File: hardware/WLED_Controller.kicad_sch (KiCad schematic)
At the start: 79 parts, among them J1 Conn_01x01_Male, J11 Conn_01x01_Male, J12 Conn_01x01_Male, J2 USB_B_Micro, J3 Conn_01x01_Male, J4 Conn_01x01_Male, J5 Conn_01x01_Male, Q1 S8050_SMD, Q2 S8050_SMD, Q3 2N7002, Q4 2N7002, SW1 SW_SPST, SW2 SW_SPST, U1 AMS1117-3.3, U2 AMS1117-3.3, U3 TP4056, U4 ESP-12F, U5 CP2102N-A01-GQFN28, U6 AP2007, U7 AP2007, U8 AP2007

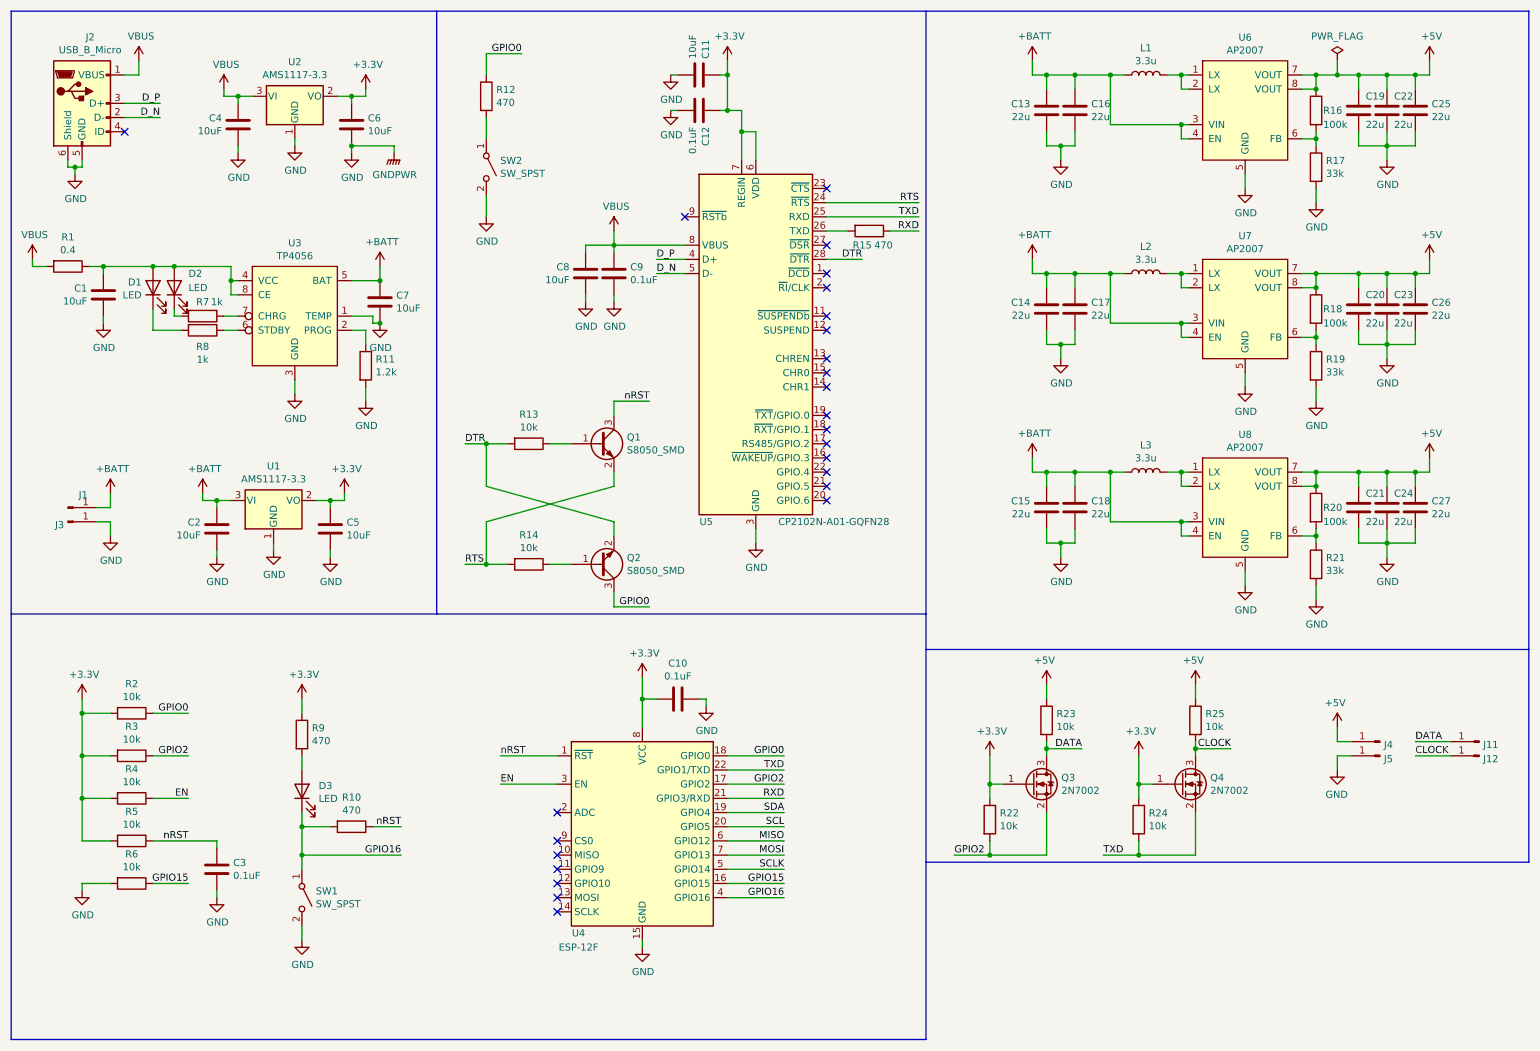
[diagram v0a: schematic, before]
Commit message: Updated to v2.0.0
Contains the PCB design and fabrication files for v2.0.0 of the WLED
controller.
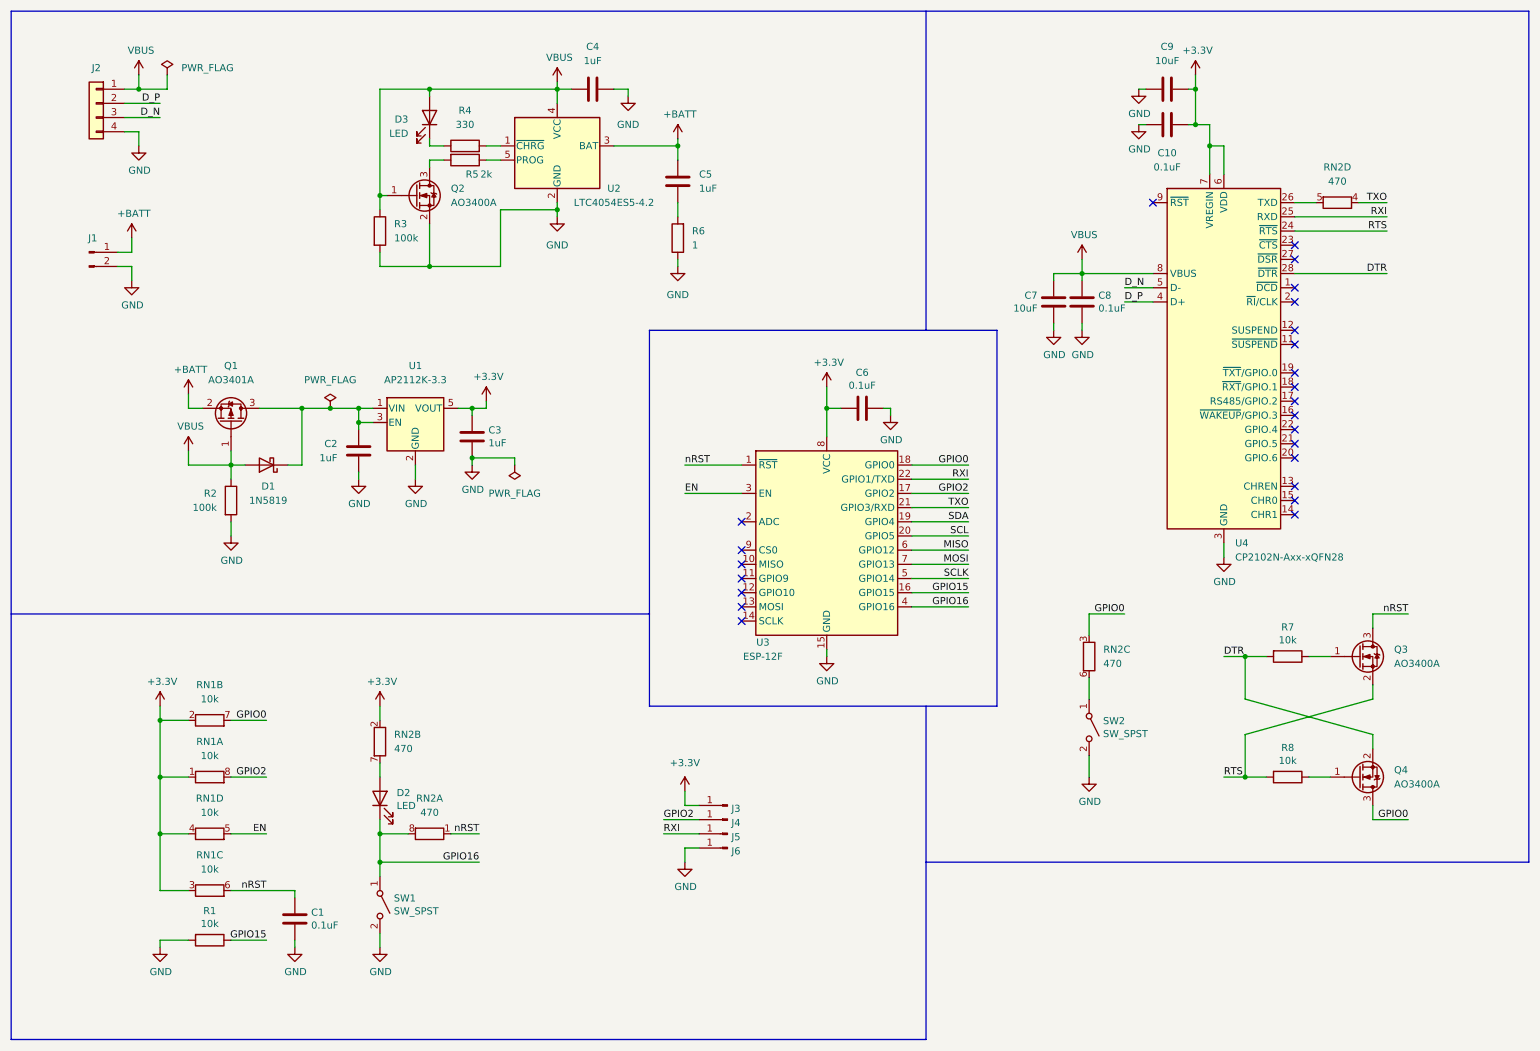
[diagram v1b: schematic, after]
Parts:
- removed C1, C11, C6: 10uF, Capacitor_SMD:C_0805_2012Metric, symbol Device:C
- removed C12: 0.1uF, Capacitor_SMD:C_0805_2012Metric, symbol Device:C
- removed C13, C14, C15, C16, C17, C18, C19, C20, C21, C22, C23, C24, C25, C26, C27: 22u, Capacitor_SMD:C_0805_2012Metric, symbol Device:C
- removed D1, D2: LED, LED_SMD:LED_0805_2012Metric, symbol Device:LED
- removed J1, J4, J5: Conn_01x01_Male, Connector_Wire:SolderWirePad_1x01_SMD_5x10mm, symbol Connector:Conn_01x01_Male
- removed J2: USB_B_Micro, Connector_USB:USB_Micro-B_Molex_47346-0001, symbol Connector:USB_B_Micro
- removed L1, L2, L3: 3.3u, Inductor_SMD:L_1206_3216Metric, symbol Device:L
- removed Q1, Q2: S8050_SMD, Package_TO_SOT_SMD:SOT-23, symbol New_Library:S8050_SMD
- removed Q3, Q4: 2N7002, Package_TO_SOT_SMD:SOT-23, symbol Transistor_FET:2N7002
- removed R1: 0.4, Resistor_SMD:R_1210_3225Metric, symbol Device:R
- removed R10, R12, R15, R9: 470, Resistor_SMD:R_0805_2012Metric, symbol Device:R
- removed R11: 1.2k, Resistor_SMD:R_0805_2012Metric, symbol Device:R
- removed R16, R18, R20: 100k, Resistor_SMD:R_0805_2012Metric, symbol Device:R
- removed R17, R19, R21: 33k, Resistor_SMD:R_0805_2012Metric, symbol Device:R
- removed R22, R23, R24, R25: 10k, Resistor_SMD:R_0805_2012Metric, symbol Device:R
- removed R7, R8: 1k, Resistor_SMD:R_0805_2012Metric, symbol Device:R
- removed U1, U2: AMS1117-3.3, Package_TO_SOT_SMD:SOT-223, symbol Regulator_Linear:AMS1117-3.3
- removed U3: TP4056, myfootprints:SOP-8-EP_3.9x4.9mm_P1.27mm, symbol New_Library:TP4056
- removed U5: CP2102N-A01-GQFN28, Package_DFN_QFN:QFN-28-1EP_5x5mm_P0.5mm_EP3.35x3.35mm, symbol Interface_USB:CP2102N-A01-GQFN28
- removed U6, U7, U8: AP2007, myfootprints:SOP-8-EP_3.9x4.9mm_P1.27mm, symbol New_Library:AP2007
- added C10: 0.1uF, Capacitor_SMD:C_0603_1608Metric, symbol Device:C
- added C3: 1uF, Capacitor_SMD:C_0603_1608Metric, symbol Device:C
- added D1: 1N5819, Diode_SMD:D_SOD-323, symbol Diode:1N5819
- added D3: LED, LED_SMD:LED_0603_1608Metric, symbol Device:LED
- added J1: Conn_01x02_Male, Connector_JST:JST_PH_S2B-PH-K_1x02_P2.00mm_Horizontal, symbol Connector:Conn_01x02_Male
- added J2: Conn_01x04, Connector_PinHeader_2.54mm:PinHeader_1x04_P2.54mm_Vertical, symbol Connector_Generic:Conn_01x04
- added J6: Conn_01x01_Male, Connector_Wire:SolderWirePad_1x01_SMD_1x2mm, symbol Connector:Conn_01x01_Male
- added Q1: AO3401A, Package_TO_SOT_SMD:SOT-23, symbol Transistor_FET:AO3401A
- added Q2, Q3, Q4: AO3400A, Package_TO_SOT_SMD:SOT-23, symbol Transistor_FET:AO3400A
- added R6: 1, Resistor_SMD:R_0603_1608Metric, symbol Device:R
- added RN1: 10k, Resistor_SMD:R_Array_Convex_4x0603, symbol Device:R_Pack04_Split
- added RN2: 470, Resistor_SMD:R_Array_Convex_4x0603, symbol Device:R_Pack04_Split
- added U1: AP2112K-3.3, Package_TO_SOT_SMD:SOT-23-5, symbol Regulator_Linear:AP2112K-3.3
- added U2: LTC4054ES5-4.2, Package_TO_SOT_SMD:TSOT-23-5, symbol Battery_Management:LTC4054ES5-4.2
- added U4: CP2102N-Axx-xQFN28, Package_DFN_QFN:QFN-28-1EP_5x5mm_P0.5mm_EP3.35x3.35mm, symbol Interface_USB:CP2102N-Axx-xQFN28
- C1: renamed from C3; footprint Capacitor_SMD:C_0805_2012Metric -> Capacitor_SMD:C_0603_1608Metric
- C2, C4, C5: value 10uF -> 1uF; footprint Capacitor_SMD:C_0805_2012Metric -> Capacitor_SMD:C_0603_1608Metric
- C6: renamed from C10; footprint Capacitor_SMD:C_0805_2012Metric -> Capacitor_SMD:C_0603_1608Metric
- C7: footprint Capacitor_SMD:C_0805_2012Metric -> Capacitor_SMD:C_0603_1608Metric
- C8: value 10uF -> 0.1uF; footprint Capacitor_SMD:C_0805_2012Metric -> Capacitor_SMD:C_0603_1608Metric
- C9: value 0.1uF -> 10uF; footprint Capacitor_SMD:C_0805_2012Metric -> Capacitor_SMD:C_0603_1608Metric
- D2: renamed from D3; footprint LED_SMD:LED_0805_2012Metric -> LED_SMD:LED_0603_1608Metric
- J3: footprint Connector_Wire:SolderWirePad_1x01_SMD_5x10mm -> Connector_Wire:SolderWirePad_1x01_SMD_1x2mm
- R1: renamed from R6; footprint Resistor_SMD:R_0805_2012Metric -> Resistor_SMD:R_0603_1608Metric
- R2, R3: value 10k -> 100k; footprint Resistor_SMD:R_0805_2012Metric -> Resistor_SMD:R_0603_1608Metric
- R4: value 10k -> 330; footprint Resistor_SMD:R_0805_2012Metric -> Resistor_SMD:R_0603_1608Metric
- R5: value 10k -> 2k; footprint Resistor_SMD:R_0805_2012Metric -> Resistor_SMD:R_0603_1608Metric
- R7: renamed from R13; footprint Resistor_SMD:R_0805_2012Metric -> Resistor_SMD:R_0603_1608Metric
- R8: renamed from R14; footprint Resistor_SMD:R_0805_2012Metric -> Resistor_SMD:R_0603_1608Metric
- SW1, SW2: footprint Button_Switch_SMD:SW_SPST_B3U-1000P -> Button_Switch_SMD:SW_SPST_TL3342
- renumbered J11 to J4, J12 to J5, U4 to U3
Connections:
- net DATA is gone; now on net GPIO2: J4.1 (Pin_1)
- net TXD is gone; now on net RXI: U3.22 (GPIO1/TXD)
- net +3V3: now also C9.1, J3.1 (Pin_1), C10.1, C3.1, RN1.1 (R1.1), RN1.2 (R2.1), RN1.3 (R3.1), RN1.4 (R4.1), RN2.2 (R2.1), U1.5 (VOUT), U4.6 (VDD), U4.7 (VREGIN); no longer C5.1, R2.2, R3.2, R4.2, R5.2
- net +BATT: now also C5.2, J1.1 (Pin_1), Q1.2 (S), U2.3 (BAT); no longer C2.1, C7.1
- net DTR: now also Q4.2 (S), U4.28 (~{DTR})
- net D_N: now also J2.3 (Pin_3), U4.5 (D-)
- net D_P: now also J2.2 (Pin_2), U4.4 (D+)
- net EN: now also RN1.5 (R4.2); no longer R4.1
- net GND: now also R2.2, R3.2, C10.2, C3.2, J1.2 (Pin_2), J2.4 (Pin_4), J6.1 (Pin_1), Q2.2 (S), R6.1, U1.2 (GND), U2.2 (GND), U4.29 (GND), U4.3 (GND); no longer C5.2, J3.1 (Pin_1)
- net GPIO0: now also Q4.3 (D), RN1.7 (R2.2), RN2.3 (R3.1); no longer R2.1
- net GPIO16: now also RN2.8 (R1.2)
- net GPIO2: now also RN1.8 (R1.2); no longer R3.1
- net RTS: now also Q3.2 (S), U4.24 (~{RTS})
- net VBUS: now also C7.1, R2.1, R3.1, D1.2 (A), D3.2 (A), J2.1 (Pin_1), Q1.1 (G), Q2.1 (G), U2.4 (VCC), U4.8 (VBUS); no longer C9.1
- net nRST: now also Q3.3 (D), RN1.6 (R3.2), RN2.1 (R1.1); no longer R5.1
- net at R7.1: now also Q3.1 (G)
- net at R8.1: now also Q4.1 (G)
- net at SW2.1 (A): now also RN2.6 (R3.2)
- net at D2.2 (A): now also RN2.7 (R2.2)
- net CLOCK renamed RXI
- net RXI: now also U4.25 (RXD)
- net RXD renamed TXO
- net TXO: now also RN2.4 (R4.1)
- new net: C2.1, D1.1 (K), Q1.3 (D), U1.1 (VIN), U1.3 (EN)
- new net: Q2.3 (D), R5.2
- new net: R5.1, U2.5 (PROG)
- new net: RN2.5 (R4.2), U4.26 (TXD)
- new net: D3.1 (K), R4.1
- new net: R4.2, U2.1 (~{CHRG})
- new net: C5.1, R6.2
- no-connect marks 25 -> 24
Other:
- moved on the sheet: C1, C6, D2, J4, J5, R1, R7, R8, SW1, SW2, U3
